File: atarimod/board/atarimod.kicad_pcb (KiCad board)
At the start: 2 copper layers, 24.1 x 50.8 mm, 15 parts, among them IC1 74HC14D, IC2 74HC14D, IC3 74HC14D, IC4 74HC14D, P1 CONN_02X20, P2 CONN_02X10, U2 APE8865N-33-HF-3

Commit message: Fixed a bug in the board layout
Working version now on Atari 800XL.
But in the mod board that needed some botching. Fixed in schematic and
layout. Removed buggy gerber files.
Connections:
- net PHI2 renamed CLK
- P1 pad 22: Net-(IC4-Pad13) -> (no net)
- P1 pad 24: (no net) -> Net-(IC4-Pad13)
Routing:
- net Net-(IC4-Pad13): track 23.3 -> 21.0 mm
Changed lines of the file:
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@@
   (net 41 "Net-(IC2-Pad13)")
   (net 42 "Net-(IC4-Pad1)")
-  (net 43 PHI2)
-  (net 44 "Net-(P2-Pad19)")
+  (net 43 "Net-(P2-Pad19)")
+  (net 44 CLK)
   (net_class Default "This is the default net class."
     (clearance 0.2)
@@
     (add_net AN1)
     (add_net AN2)
+    (add_net CLK)
     (add_net CS)
     (add_net D0)
@@
     (add_net "Net-(IC4-Pad5)")
     (add_net "Net-(P2-Pad19)")
-    (add_net PHI2)
     (add_net RW)
   )
@@
       (net 36 "Net-(IC4-Pad11)"))
     (pad 12 smd rect (at 2.7 -1.27) (size 1.5 0.6) (layers F.Cu F.Paste F.Mask)
-      (net 43 PHI2))
+      (net 44 CLK))
     (pad 13 smd rect (at 2.7 -2.54) (size 1.5 0.6) (layers F.Cu F.Paste F.Mask)
       (net 38 "Net-(IC4-Pad13)"))
@@
     (pad 20 thru_hole oval (at 2.54 22.86) (size 1.7 1.7) (drill 1) (layers *.Cu *.Mask))
     (pad 21 thru_hole oval (at 0 25.4) (size 1.7 1.7) (drill 1) (layers *.Cu *.Mask))
-    (pad 22 thru_hole oval (at 2.54 25.4) (size 1.7 1.7) (drill 1) (layers *.Cu *.Mask)
+    (pad 22 thru_hole oval (at 2.54 25.4) (size 1.7 1.7) (drill 1) (layers *.Cu *.Mask))
+    (pad 23 thru_hole oval (at 0 27.94) (size 1.7 1.7) (drill 1) (layers *.Cu *.Mask))
+    (pad 24 thru_hole oval (at 2.54 27.94) (size 1.7 1.7) (drill 1) (layers *.Cu *.Mask)
       (net 38 "Net-(IC4-Pad13)"))
-    (pad 23 thru_hole oval (at 0 27.94) (size 1.7 1.7) (drill 1) (layers *.Cu *.Mask))
-    (pad 24 thru_hole oval (at 2.54 27.94) (size 1.7 1.7) (drill 1) (layers *.Cu *.Mask))
     (pad 25 thru_hole oval (at 0 30.48) (size 1.7 1.7) (drill 1) (layers *.Cu *.Mask))
     (pad 26 thru_hole oval (at 2.54 30.48) (size 1.7 1.7) (drill 1) (layers *.Cu *.Mask))
@@
       (net 35 CS))
     (pad 19 thru_hole oval (at 0 22.86) (size 1.7 1.7) (drill 1) (layers *.Cu *.Mask)
-      (net 44 "Net-(P2-Pad19)"))
+      (net 43 "Net-(P2-Pad19)"))
     (pad 20 thru_hole oval (at 2.54 22.86) (size 1.7 1.7) (drill 1) (layers *.Cu *.Mask)
       (net 37 HALT))
@@
     (fp_line (start 2.35 0.9) (end -2.35 0.9) (layer F.CrtYd) (width 0.05))
     (pad 1 smd rect (at -1.35 0 270) (size 1.5 1.3) (layers F.Cu F.Paste F.Mask)
-      (net 44 "Net-(P2-Pad19)"))
+      (net 43 "Net-(P2-Pad19)"))
     (pad 2 smd rect (at 1.35 0 270) (size 1.5 1.3) (layers F.Cu F.Paste F.Mask)
-      (net 43 PHI2))
+      (net 44 CLK))
     (model ${KISYS3DMOD}/Resistors_SMD.3dshapes/R_0805.wrl
       (at (xyz 0 0 0))
@@
   (segment (start 130.81 126.238) (end 130.81 111.76) (width 0.25) (layer F.Cu) (net 37))
   (segment (start 127.508 129.54) (end 130.81 126.238) (width 0.25) (layer F.Cu) (net 37))
+  (segment (start 111.76 111.76) (end 112.522 111.76) (width 0.25) (layer F.Cu) (net 38))
+  (segment (start 112.522 111.76) (end 114.046 113.284) (width 0.25) (layer F.Cu) (net 38))
   (segment (start 122.08 125.73) (end 121.158 125.73) (width 0.25) (layer F.Cu) (net 38))
-  (segment (start 114.046 111.252) (end 112.014 109.22) (width 0.25) (layer F.Cu) (net 38))
-  (segment (start 114.046 115.316) (end 114.046 111.252) (width 0.25) (layer F.Cu) (net 38))
+  (segment (start 114.046 115.316) (end 114.046 113.284) (width 0.25) (layer F.Cu) (net 38))
   (via (at 114.046 115.316) (size 0.6) (drill 0.4) (layers F.Cu B.Cu) (net 38))
   (segment (start 114.046 119.126) (end 114.046 115.316) (width 0.25) (layer B.Cu) (net 38))
@@
   (via (at 120.396 124.968) (size 0.6) (drill 0.4) (layers F.Cu B.Cu) (net 38))
   (segment (start 121.158 125.73) (end 120.396 124.968) (width 0.25) (layer F.Cu) (net 38))
-  (segment (start 112.014 109.22) (end 111.76 109.22) (width 0.25) (layer F.Cu) (net 38))
   (segment (start 111.76 96.52) (end 112.268 96.52) (width 0.25) (layer F.Cu) (net 39))
   (segment (start 112.268 96.52) (end 115.062 99.314) (width 0.25) (layer F.Cu) (net 39))
@@
   (segment (start 116.84 95.25) (end 117.348 95.25) (width 0.25) (layer F.Cu) (net 41))
   (segment (start 113.03 91.44) (end 116.84 95.25) (width 0.25) (layer F.Cu) (net 41))
-  (segment (start 116.68 124.46) (end 115.062 124.46) (width 0.25) (layer F.Cu) (net 42) (status 400000))
+  (segment (start 116.68 124.46) (end 115.062 124.46) (width 0.25) (layer F.Cu) (net 42))
   (segment (start 110.49 125.73) (end 109.22 127) (width 0.25) (layer F.Cu) (net 42))
   (segment (start 113.792 125.73) (end 114.554 124.968) (width 0.25) (layer F.Cu) (net 42))
   (segment (start 110.49 125.73) (end 113.792 125.73) (width 0.25) (layer F.Cu) (net 42))
   (segment (start 115.062 124.46) (end 114.554 124.968) (width 0.25) (layer F.Cu) (net 42))
-  (segment (start 128.27 117.936) (end 128.27 125.65) (width 0.25) (layer F.Cu) (net 43))
-  (segment (start 128.27 125.65) (end 126.92 127) (width 0.25) (layer F.Cu) (net 43))
-  (segment (start 122.08 127) (end 126.92 127) (width 0.25) (layer F.Cu) (net 43))
-  (segment (start 128.27 111.76) (end 128.27 115.236) (width 0.25) (layer F.Cu) (net 44))
+  (segment (start 128.27 111.76) (end 128.27 115.236) (width 0.25) (layer F.Cu) (net 43))
+  (segment (start 128.27 117.936) (end 128.27 125.65) (width 0.25) (layer F.Cu) (net 44))
+  (segment (start 128.27 125.65) (end 126.92 127) (width 0.25) (layer F.Cu) (net 44))
+  (segment (start 122.08 127) (end 126.92 127) (width 0.25) (layer F.Cu) (net 44))
 )

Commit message: Revision 3 of Atari GTIA Adapter
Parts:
- removed REF***: OSHW-Logo2_9.8x8mm_SilkScreen, Symbols:OSHW-Logo2_9.8x8mm_SilkScreen
- C1, C2: value 10uF -> 1uF; footprint Capacitors_SMD:C_0805_HandSoldering -> Capacitor_SMD:C_0805_2012Metric_Pad1.15x1.40mm_HandSolder
- C3, C4, C5, C6: footprint Capacitors_SMD:C_0603_HandSoldering -> Capacitor_SMD:C_0603_1608Metric_Pad1.05x0.95mm_HandSolder
- IC1, IC2, IC3, IC4: value 74HC14D -> SN74LVC14ADBR; footprint Housings_SOIC:SOIC-14_3.9x8.7mm_Pitch1.27mm -> Package_SO:SSOP-14_5.3x6.2mm_P0.65mm
- P1: value CONN_02X20 -> DIP40_Socket; footprint Pin_Headers:Pin_Header_Straight_2x20_Pitch2.54mm -> ProjectFootprints:socket_embedded_40pin
- P2: footprint Pin_Headers:Pin_Header_Angled_2x10_Pitch2.54mm -> Connector_PinHeader_2.54mm:PinHeader_2x10_P2.54mm_Vertical
- R10: footprint Resistors_SMD:R_0805_HandSoldering -> Resistor_SMD:R_0805_2012Metric_Pad1.15x1.40mm_HandSolder
- U2: value APE8865N-33-HF-3 -> RT9166-33GVL; footprint TO_SOT_Packages_SMD:SOT-23 -> Package_TO_SOT_SMD:SOT-23
- moved C1 35.8 mm to (144.1, 99.1), turned to 0 degrees
- moved U2 29.4 mm to (144.1, 103.5), turned to 90 degrees
- moved IC4 29.1 mm to (132.1, 102.1)
- moved C6 28.8 mm to (131.6, 96.5)
- moved IC3 27.3 mm to (132.1, 87.6)
- moved C5 26.1 mm to (132.1, 83.2)
- moved IC2 25.6 mm to (132.1, 78.1)
- moved C4 24.4 mm to (132.1, 73.7)
- moved IC1 24.0 mm to (132.1, 68.6)
- moved C2 23.9 mm to (144.1, 108.0), turned to 180 degrees
- moved P2 23.0 mm to (142.9, 71.1)
- moved P1 22.9 mm to (132.1, 83.8), turned to 270 degrees
- moved C3 22.8 mm to (132.1, 64.1)
- moved R10 21.6 mm to (135.7, 96.3), turned to 180 degrees
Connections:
- IC1 pad 6: (no net) -> Net-(IC1-Pad6)
- IC3 pad 4: (no net) -> Net-(IC3-Pad4)
- IC3 pad 6: (no net) -> Net-(IC3-Pad6)
- IC4 pad 8: (no net) -> Net-(IC4-Pad8)
- P1 pad 10: Net-(IC2-Pad11) -> Net-(P1-Pad10)
- P1 pad 11: Net-(IC2-Pad5) -> Net-(P1-Pad11)
- P1 pad 12: Net-(IC2-Pad9) -> Net-(P1-Pad12)
- P1 pad 13: Net-(IC3-Pad1) -> Net-(P1-Pad13)
- P1 pad 14: Net-(IC3-Pad13) -> Net-(P1-Pad14)
- P1 pad 15: (no net) -> Net-(P1-Pad15)
- P1 pad 16: Net-(IC3-Pad11) -> Net-(P1-Pad16)
- P1 pad 17: (no net) -> Net-(P1-Pad17)
- P1 pad 18: Net-(IC3-Pad9) -> Net-(IC4-Pad1)
- P1 pad 19: (no net) -> Net-(IC4-Pad3)
- P1 pad 2: Net-(IC1-Pad13) -> Net-(IC1-Pad3)
- P1 pad 20: (no net) -> Net-(IC4-Pad5)
- P1 pad 21: (no net) -> Net-(P1-Pad21)
- P1 pad 22: (no net) -> Net-(P1-Pad22)
- P1 pad 23: (no net) -> Net-(P1-Pad23)
- P1 pad 24: Net-(IC4-Pad13) -> Net-(P1-Pad24)
- P1 pad 25: (no net) -> Net-(P1-Pad25)
- P1 pad 26: (no net) -> Net-(IC4-Pad11)
- P1 pad 27: (no net) -> +5V
- P1 pad 28: +5V -> Net-(P1-Pad28)
- P1 pad 29: (no net) -> Net-(IC4-Pad13)
- P1 pad 3: Net-(IC1-Pad3) -> GND
- P1 pad 30: Net-(IC4-Pad11) -> Net-(P1-Pad30)
- P1 pad 31: (no net) -> Net-(P1-Pad31)
- P1 pad 32: (no net) -> Net-(IC3-Pad9)
- P1 pad 33: (no net) -> Net-(IC3-Pad11)
- P1 pad 34: (no net) -> Net-(IC3-Pad13)
- P1 pad 35: Net-(IC4-Pad1) -> Net-(IC2-Pad9)
- P1 pad 36: (no net) -> Net-(IC2-Pad11)
- P1 pad 37: Net-(IC4-Pad3) -> Net-(IC2-Pad13)
- P1 pad 38: (no net) -> Net-(IC1-Pad9)
- P1 pad 39: Net-(IC4-Pad5) -> Net-(IC1-Pad11)
- P1 pad 4: Net-(IC1-Pad11) -> Net-(IC2-Pad1)
- P1 pad 40: (no net) -> Net-(IC1-Pad13)
- P1 pad 5: GND -> Net-(IC2-Pad3)
- P1 pad 6: Net-(IC1-Pad9) -> Net-(IC2-Pad5)
- P1 pad 7: Net-(IC2-Pad1) -> Net-(IC3-Pad1)
- P1 pad 8: Net-(IC2-Pad13) -> Net-(P1-Pad8)
- P1 pad 9: Net-(IC2-Pad3) -> Net-(P1-Pad9)
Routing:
- net +3V3: track 67.2 -> 126.2 mm
- net GND: track 91.0 -> 32.8 mm, vias 2 -> 10
- net A2: track 9.26 -> 20.6 mm
- net HALT: track 24.6 -> 14.3 mm, vias 0 -> 1
- net AN2: track 32.0 -> 22.0 mm, vias 1 -> 2
- net A3: track 9.26 -> 19.2 mm
- net AN1: track 30.8 -> 22.5 mm, vias 1 -> 2
- net Net-(IC4-Pad11): track 15.9 -> 7.81 mm, vias 2 -> 0
- net CLK: track 14.5 -> 6.80 mm, vias 0 -> 2
- net AN0: track 30.7 -> 23.1 mm, vias 1 -> 2
- net D5: track 9.78 -> 17.1 mm, vias 0 -> 1
- net Net-(P2-Pad19): track 3.48 -> 9.99 mm, vias 0 -> 1
- net A4: track 9.26 -> 15.6 mm, vias 0 -> 1
- net D6: track 9.78 -> 15.9 mm, vias 0 -> 1
- net Net-(IC3-Pad9): track 16.5 -> 10.8 mm, vias 2 -> 0
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- added copper zone on B.Cu, net GND
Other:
- board size 24.1 x 50.8 mm -> 25.4 x 52.1 mm
- board text added: "1"
- board text added: "Atari GTIA Adapter Rev. 3 github.com/c0pperdragon/A-VideoBoard"

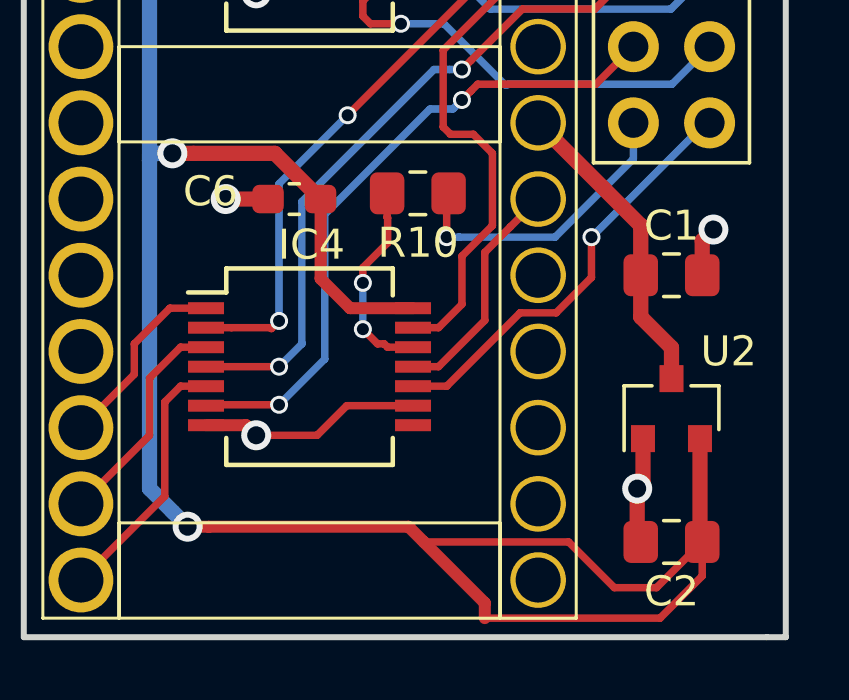
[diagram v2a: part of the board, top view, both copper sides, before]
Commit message: Use different voltage regulator to reduce noise
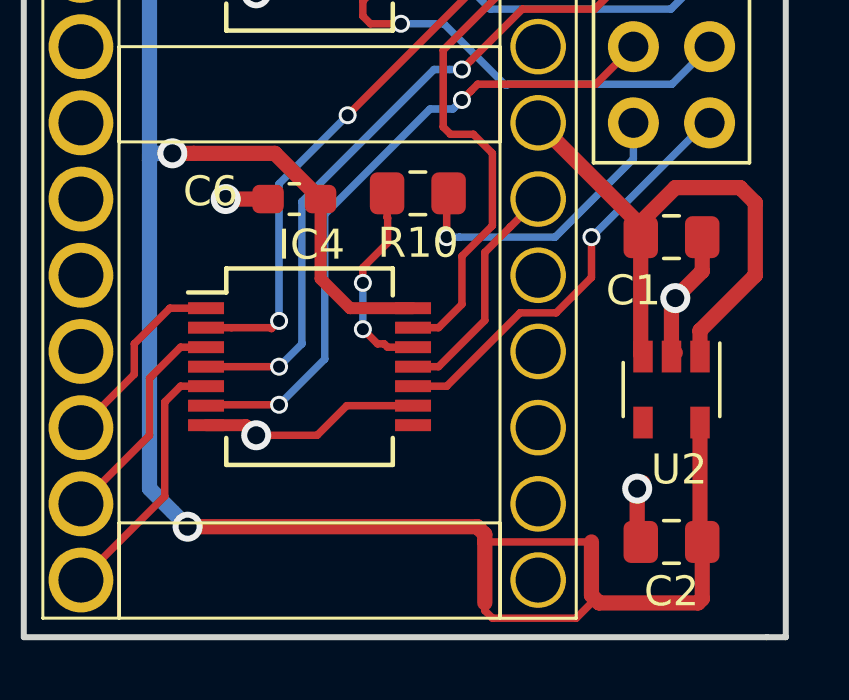
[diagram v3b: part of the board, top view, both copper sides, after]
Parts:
- C1, C2: value 1uF -> 10uF
- U2: value RT9166-33GVL -> MIC5504-3.3YM5; footprint Package_TO_SOT_SMD:SOT-23 -> Package_TO_SOT_SMD:SOT-23-5
- moved C1 1.27 mm to (144.1, 97.8)
- moved U2 0.63 mm to (144.1, 102.9), turned to 270 degrees
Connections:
- U2 pad 1: GND -> +5V
- U2 pad 2: +3V3 -> GND
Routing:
- net +5V: track 10.4 -> 20.1 mm
- net +3V3: track 126.2 -> 123.5 mm
- net GND: track 32.8 -> 34.2 mm
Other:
- board text added: "Atari GTIA Adapter Rev. 4 github.com/c0pperdragon/A-VideoBoard"
- board text removed: "Atari GTIA Adapter Rev. 3 github.com/c0pperdragon/A-VideoBoard"
